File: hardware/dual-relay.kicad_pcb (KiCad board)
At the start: 2 copper layers, 45 x 45 mm, 38 parts, among them J101 AKL_5_2, J102 AKL_5_2, J103 AKL_5_2, P101 CON-SENSOR2, P102 BOOT, Q101 2N7002P, Q102 2N7002P, U101 XMC1XXX24, U102 DRILL, U103 DRILL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

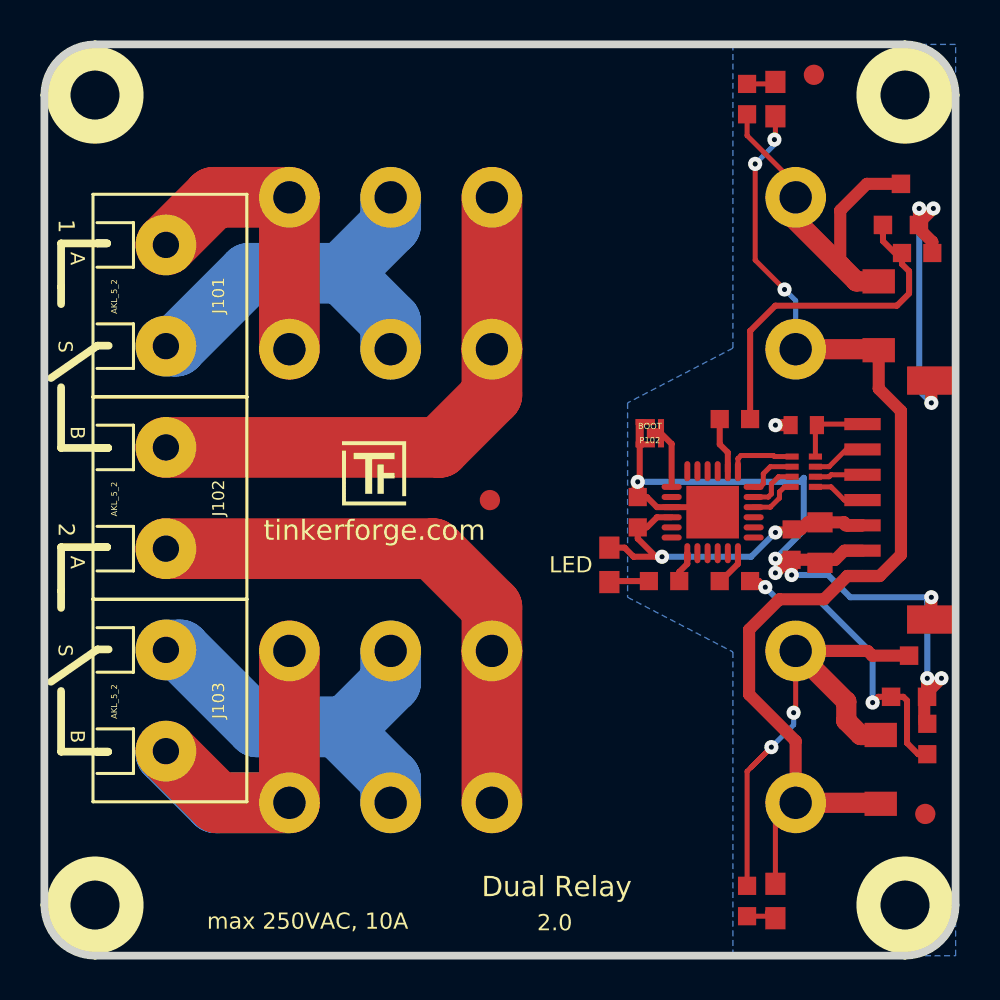
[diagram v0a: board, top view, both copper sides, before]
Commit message: industrial dual relay bricklet prototype finished
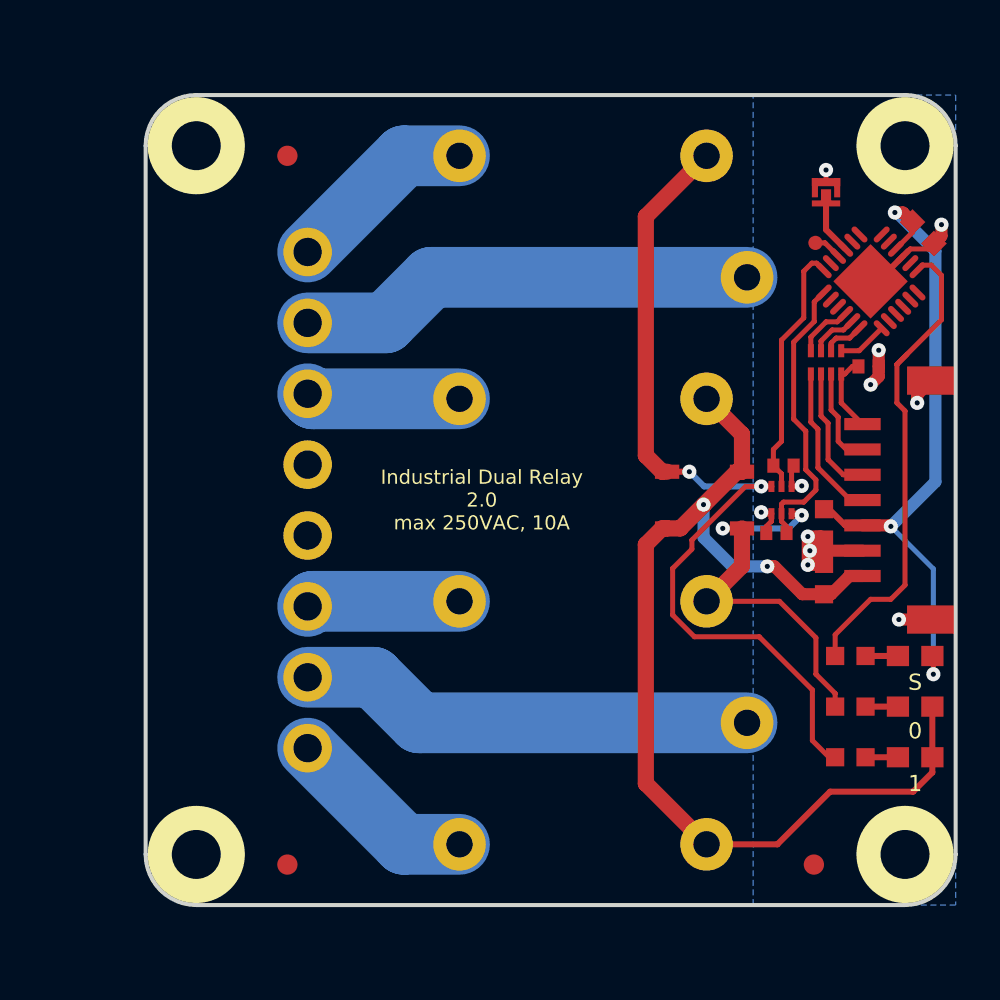
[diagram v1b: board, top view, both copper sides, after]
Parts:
- removed C101: 1uF, C0603F
- removed C102: 1uF, C0402E
- removed C103: 10uF, C0805
- removed C104: 100nF, C0603F
- removed D101, D104, D105: blue, D0603E
- removed D102, D103: LL4148, MiniMelf
- removed the Fiducial_Mark at (170.6, 119.7)
- removed the Fiducial_Mark at (165.1, 83.2)
- removed the Fiducial_Mark at (149.1, 104.2)
- removed the G*** at (160.6, 104.2)
- removed J101, J102, J103: AKL_5_2, AKL_5_2
- removed P101: CON-SENSOR2, kicad-libraries:CON-SENSOR2
- removed P102: BOOT, kicad-libraries:SolderJumper
- removed Q101, Q102: 2N7002P, SOT23GDS
- removed R101, R106, R107: 1k, R0603F
- removed R102, R103: 10, R0603F
- removed R104, R105: 10k, R0603F
- removed REL101, REL102: RELAY_29_127, RELAY_29_127
- removed RP101: TBD, kicad-libraries:4X0402
- removed U101: XMC1XXX24, kicad-libraries:QFN24-4x4mm-0.5mm
- removed U102, U103, U104, U105: DRILL, DRILL_NP
- added C1: 1uF, C0603F, F.Cu at (165.6, 108.1)
- added C2: 1uF, C0402F, F.Cu at (167.8, 97.6)
- added C3: 1uF, C0603F, F.Cu at (165.6, 105.4)
- added C4: 100nF, C0603F, F.Cu at (170.5, 91.0)
- added D1: blue, D0603E, F.Cu at (170.1, 111.9)
- added D2: blue, D0603E, F.Cu at (170.1, 116.9)
- added D3: blue, D0603E, F.Cu at (170.1, 114.4)
- added D4: LL4148, SOD-123, F.Cu at (159.7, 102.8)
- added D5: LL4148, SOD-123, F.Cu at (159.7, 105.6)
- added Fiducial_Mark: VAL**, kicad-libraries:Fiducial_Mark, F.Cu at (139.1, 87.2)
- added Fiducial_Mark: VAL**, kicad-libraries:Fiducial_Mark, F.Cu at (165.1, 122.2)
- added Fiducial_Mark: VAL**, kicad-libraries:Fiducial_Mark, F.Cu at (139.1, 122.2)
- added P1: CON-SENSOR2, CON-SENSOR2, F.Cu at (172.1, 104.2)
- added P2: BOOT, kicad-libraries:SolderJumper, F.Cu at (165.7, 89.0)
- added P3: CONN_8, kicad-libraries:OQ_8P, F.Cu at (140.1, 104.2)
- added P4: Debug, kicad-libraries:DEBUG_PAD, F.Cu at (165.2, 91.5)
- added Q1: SSM6N7002KFU, kicad-libraries:SOT563, F.Cu at (163.5, 104.2)
- added R1: 1k, R0603F, F.Cu at (166.9, 111.9)
- added R2: 1k, R0603F, F.Cu at (166.9, 116.9)
- added R3: 1k, R0603F, F.Cu at (166.9, 114.4)
- added R4: 10k, kicad-libraries:R0402F, F.Cu at (163.2, 105.8)
- added R5: 10k, kicad-libraries:R0402F, F.Cu at (163.6, 102.5)
- added RP1: TBD, kicad-libraries:4X0402, F.Cu at (165.7, 97.4)
- added U1: XMC1XXX24, kicad-libraries:QFN24-4x4mm-0.5mm, F.Cu at (167.9, 93.4)
- added U2: G5LE-1-36, G5LE-1, F.Cu at (153.1, 93.2)
- added U3: G5LE-1-36, G5LE-1, F.Cu at (153.1, 115.2)
- added U4: DRILL, DRILL_NP, F.Cu at (169.6, 121.7)
- added U5: DRILL, DRILL_NP, F.Cu at (134.6, 121.7)
- added U6: DRILL, DRILL_NP, F.Cu at (134.6, 86.7)
- added U7: DRILL, DRILL_NP, F.Cu at (169.6, 86.7)
- added VAL: WEEE_7mm, kicad-libraries:WEEE_7mm, B.Cu at (152.1, 108.2)
- G***: moved to B.Cu
- moved G*** 17.7 mm to (153.7, 114.4), turned to 180 degrees
- moved G*** 13.0 mm to (152.1, 91.2)
- moved VAL 10.3 mm to (152.1, 100.2)
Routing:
- net Net-(D4-Pad1): track 0.00 -> 44.5 mm, vias 0 -> 2
- net GND: track 61.8 -> 28.2 mm
- net Net-(J102-Pad1): track 27.0 -> 0.00 mm
- net Net-(J102-Pad2): track 26.9 -> 0.00 mm
- net Net-(D103-Pad1): track 26.2 -> 0.00 mm, vias 2 -> 0
- net Net-(R1-Pad1): track 0.00 -> 24.1 mm
- net Net-(P3-Pad7): track 0.00 -> 22.6 mm
- net Net-(P3-Pad2): track 0.00 -> 22.6 mm
- net Net-(J103-Pad1): track 21.9 -> 0.00 mm
- net Net-(D5-Pad1): track 0.00 -> 20.8 mm, vias 0 -> 2
- net Net-(J103-Pad2): track 20.0 -> 0.00 mm
- net Net-(J101-Pad1): track 19.7 -> 0.00 mm
- net Net-(D102-Pad1): track 18.0 -> 0.00 mm
- net Net-(Q101-PadG): track 17.2 -> 0.00 mm
- net Net-(Q102-PadG): track 15.4 -> 0.00 mm, vias 2 -> 0
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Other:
- board size 45 x 45 mm -> 40 x 40 mm
- board text added: "0"
- board text added: "Industrial Dual Relay 2.0 max 250VAC, 10A"
- board text removed: "2"
- board text removed: "2.0"
- board text removed: "Dual Relay"
- board text removed: "LED"
- board text removed: "max 250VAC, 10A"

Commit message: fix description text
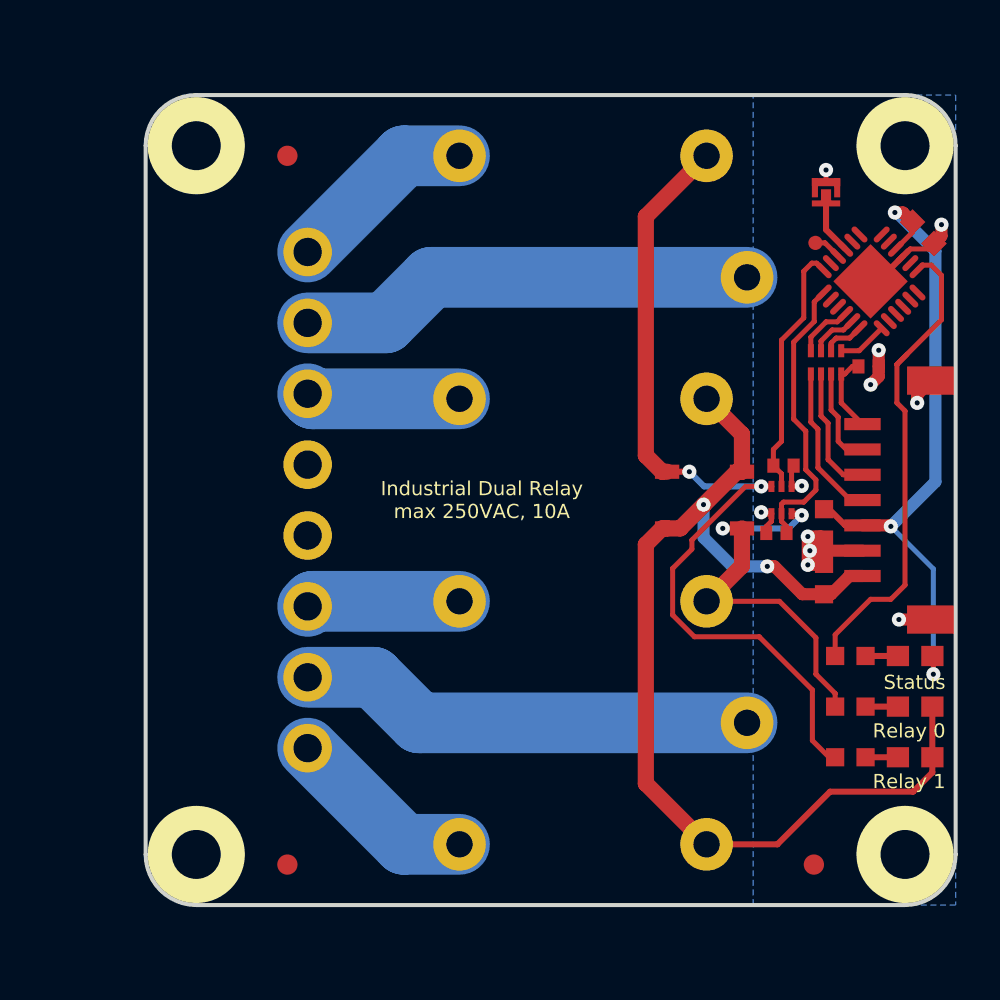
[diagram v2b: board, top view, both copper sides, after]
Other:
- board text added: "Industrial Dual Relay max 250VAC, 10A"
- board text added: "Relay 0"
- board text added: "Relay 1"
- board text added: "Status"
- board text removed: "Industrial Dual Relay 2.0 max 250VAC, 10A"
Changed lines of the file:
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@@
     (links 61)
     (no_connects 0)
-    (area 131.973659 84.071159 172.175001 124.275001)
+    (area 131.220139 83.320139 282.19527 165.489573)
     (thickness 1.6002)
     (drawings 34)
@@
   (layers
     (0 Vorderseite signal)
-    (31 Rückseite signal)
+    (31 Rückseite signal hide)
     (32 B.Adhes user)
     (33 F.Adhes user)
@@
   (gr_line (start 136.075 109.475) (end 133.675 109.475) (angle 90) (layer B.SilkS) (width 0.381))
   (gr_line (start 135.5 112.975) (end 134.15 114.325) (angle 90) (layer B.SilkS) (width 0.381))
-  (gr_text S (at 170.075 113.175) (layer F.SilkS)
-    (effects (font (size 0.8001 0.8001) (thickness 0.14986)))
+  (gr_text Status (at 171.575 113.175) (layer F.SilkS)
+    (effects (font (size 0.7 0.7) (thickness 0.14986)) (justify right))
   )
-  (gr_text 1 (at 170.075 118.175) (layer F.SilkS)
-    (effects (font (size 0.8001 0.8001) (thickness 0.14986)))
+  (gr_text "Relay 1" (at 171.575 118.075) (layer F.SilkS)
+    (effects (font (size 0.7 0.7) (thickness 0.14986)) (justify right))
   )
   (gr_line (start 172.075 121.675) (end 172.075 86.675) (angle 90) (layer Edge.Cuts) (width 0.2))
@@
   (gr_line (start 132.075 86.675) (end 132.075 121.675) (angle 90) (layer Edge.Cuts) (width 0.2))
   (gr_line (start 169.575 84.175) (end 134.575 84.175) (angle 90) (layer Edge.Cuts) (width 0.2))
-  (gr_text 0 (at 170.075 115.575) (layer F.SilkS)
-    (effects (font (size 0.8001 0.8001) (thickness 0.14986)))
+  (gr_text "Relay 0" (at 171.575 115.575) (layer F.SilkS)
+    (effects (font (size 0.7 0.7) (thickness 0.14986)) (justify right))
   )
   (gr_text A (at 134.475 110.175 270) (layer B.SilkS)
@@
   (gr_arc (start 169.57294 121.67298) (end 172.0723 121.67298) (angle 90) (layer Edge.Cuts) (width 0.2))
   (gr_arc (start 169.57294 86.67306) (end 169.57294 84.17116) (angle 90) (layer Edge.Cuts) (width 0.2))
-  (gr_text "Industrial Dual Relay\n2.0\nmax 250VAC, 10A" (at 148.675 104.175) (layer F.SilkS)
+  (gr_text "Industrial Dual Relay\nmax 250VAC, 10A" (at 148.675 104.175) (layer F.SilkS)
     (effects (font (size 0.7 0.7) (thickness 0.15)))
   )

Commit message: specify values
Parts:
- C2: value 1uF -> 220pF
- RP1: value TBD -> 82
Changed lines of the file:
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@@
     (links 61)
     (no_connects 0)
-    (area 131.220139 83.320139 282.19527 165.489573)
+    (area 131.973659 84.071159 172.175001 124.275001)
     (thickness 1.6002)
     (drawings 34)
@@
       (effects (font (size 0.2 0.2) (thickness 0.05)))
     )
-    (fp_text value TBD (at -0.025 -0.45) (layer F.Fab)
+    (fp_text value 82 (at -0.025 -0.45) (layer F.Fab)
       (effects (font (size 0.2 0.2) (thickness 0.05)))
     )
@@
       (effects (font (size 0.2 0.2) (thickness 0.05)))
     )
-    (fp_text value 1uF (at 0 -0.15 180) (layer F.Fab)
-      (effects (font (size 0.2 0.2) (thickness 0.05)))
-    )
+    (fp_text value 220pF (at 0 -0.15 180) (layer F.Fab)
+      (effects (font (size 0.2 0.2) (thickness 0.05)))
+    )

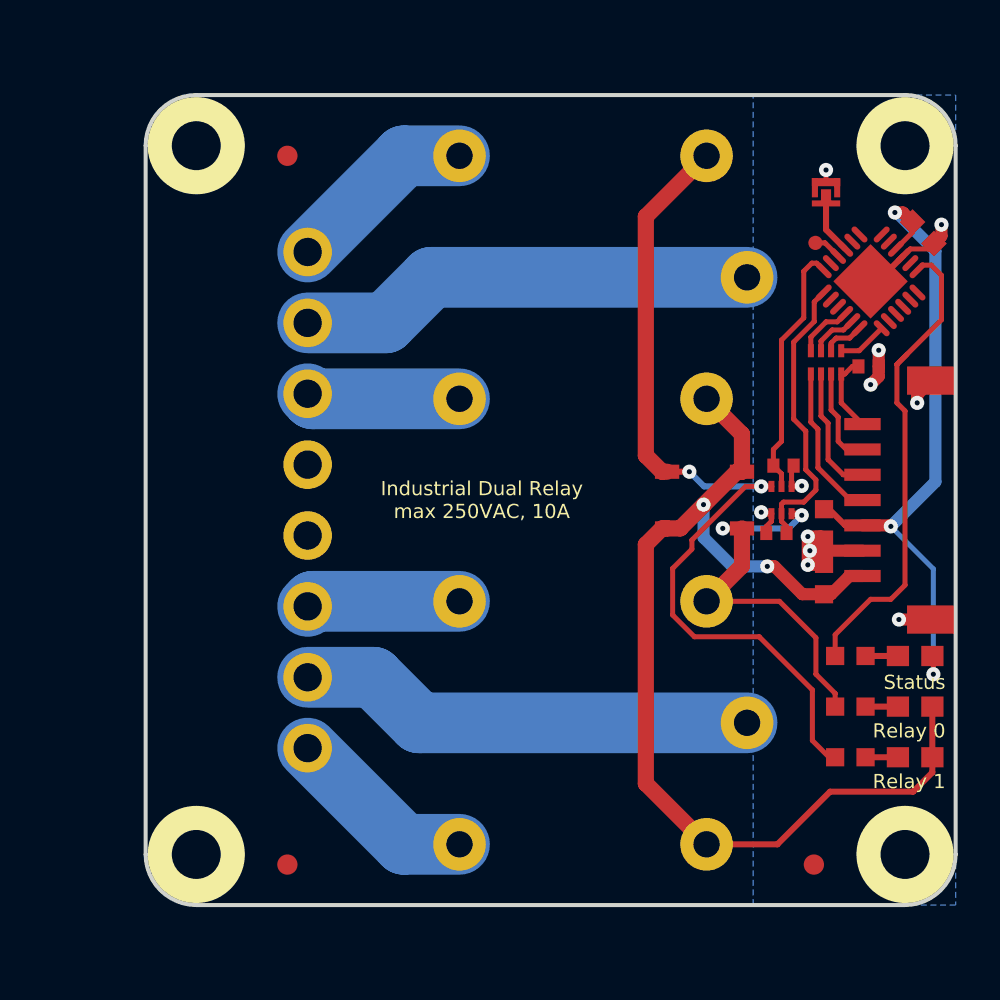
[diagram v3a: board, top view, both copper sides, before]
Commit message: fix mosfet footprint
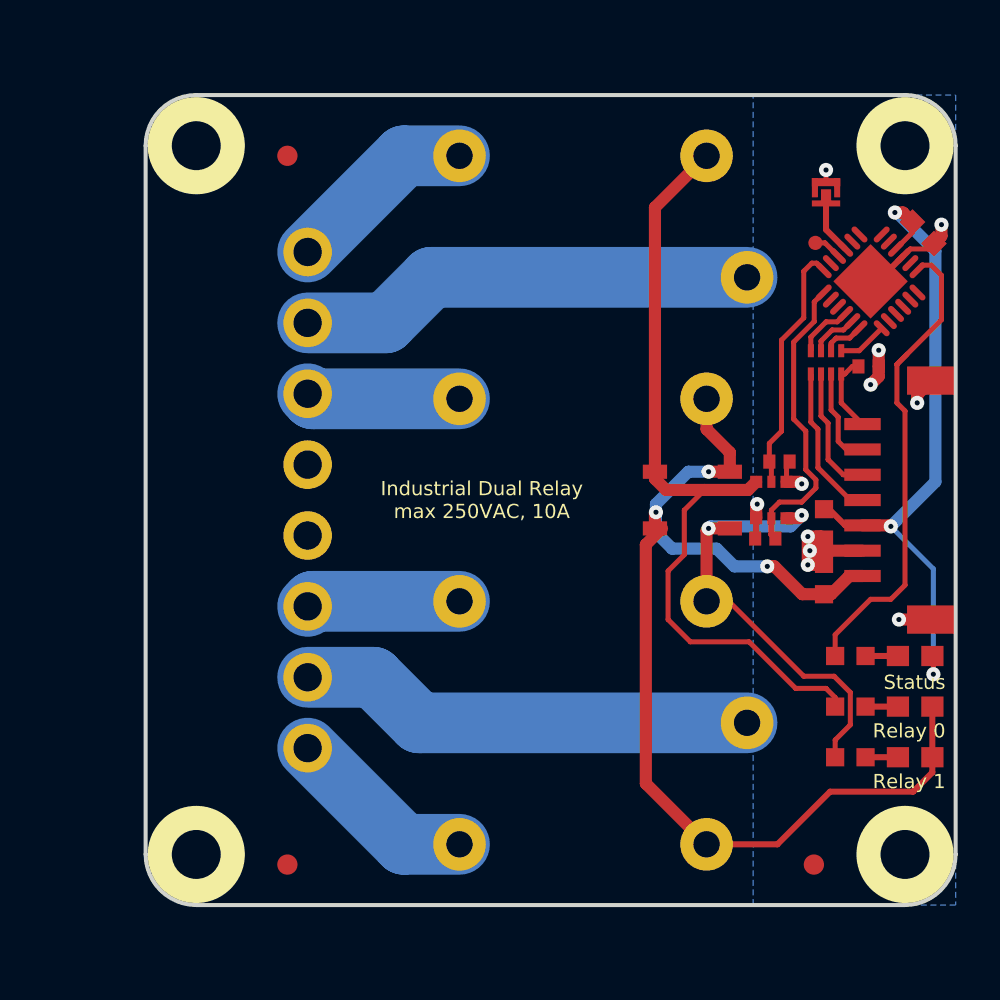
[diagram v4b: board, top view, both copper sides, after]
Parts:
- Q1: footprint kicad-libraries:SOT563 -> kicad-libraries:SOT363
- R4, R5: footprint kicad-libraries:R0402F -> R0402F
- moved D2 2.50 mm to (170.1, 114.4)
- moved D3 2.50 mm to (170.1, 116.9)
- moved R2 2.50 mm to (166.9, 114.4)
- moved R3 2.50 mm to (166.9, 116.9)
- moved R4 0.61 mm to (162.7, 106.1)
- moved D4 0.60 mm to (159.1, 102.8)
- moved D5 0.60 mm to (159.1, 105.6)
- moved Q1 0.50 mm to (163.0, 104.2), turned to 90 degrees
- moved R5 0.28 mm to (163.4, 102.3)
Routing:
- net Net-(D5-Pad1): track 20.8 -> 25.9 mm
- net Net-(D4-Pad1): track 44.5 -> 39.8 mm, vias 2 -> 0
- net +5V: track 53.5 -> 55.5 mm, vias 2 -> 3
- net RELAY1: track 14.3 -> 14.9 mm

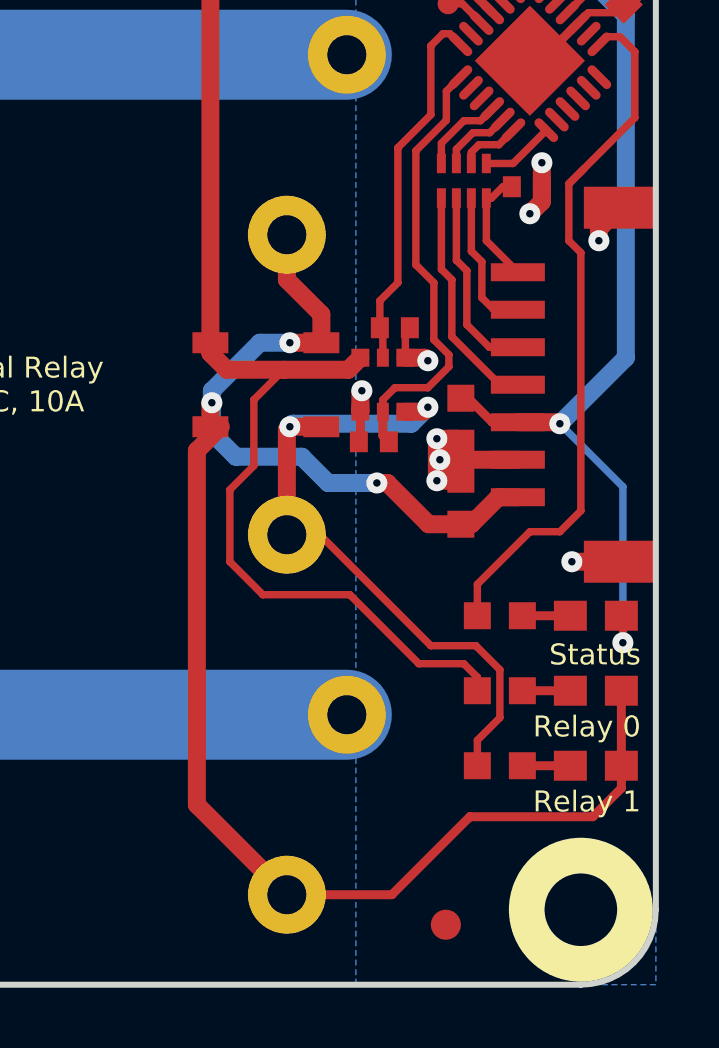
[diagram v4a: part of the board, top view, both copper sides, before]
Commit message: fix logo positions
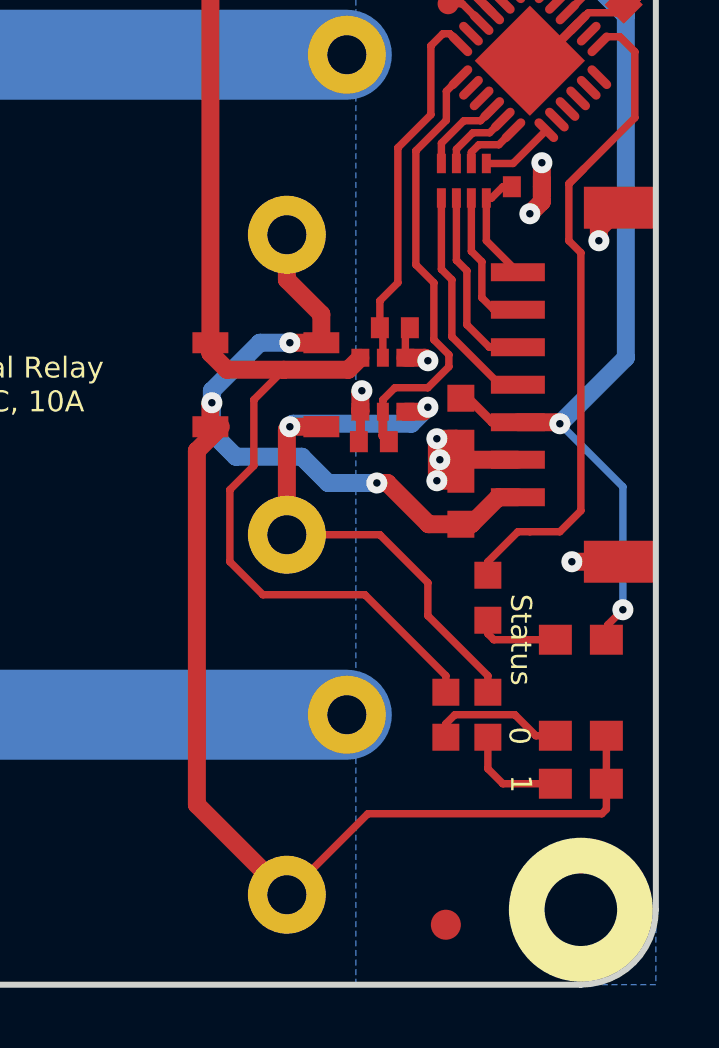
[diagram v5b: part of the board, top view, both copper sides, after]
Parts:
- moved G*** 23.0 mm to (152.1, 114.2), turned to 90 degrees
- moved G*** 18.8 mm to (170.4, 105.8), turned to 90 degrees
- moved VAL 6.00 mm to (152.1, 94.2), turned to 90 degrees
- moved VAL 4.00 mm to (152.1, 104.2), turned to 90 degrees
- moved R2 1.97 mm to (165.1, 115.2), turned to 270 degrees
- moved R3 1.75 mm to (166.5, 115.2), turned to 270 degrees
- moved D2 1.58 mm to (169.6, 115.9)
- moved D1 0.94 mm to (169.6, 112.7)
- moved D3 0.78 mm to (169.6, 117.5)
- moved R1 0.72 mm to (166.5, 111.3), turned to 270 degrees
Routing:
- net Net-(D2-Pad2): track 1.60 -> 4.51 mm
- net Net-(D3-Pad2): track 1.60 -> 3.51 mm
- net +5V: track 55.5 -> 53.9 mm
- net Net-(D5-Pad1): track 25.9 -> 24.4 mm
- net Net-(R1-Pad1): track 24.1 -> 22.8 mm
- net Net-(D1-Pad2): track 1.60 -> 2.78 mm
- net Net-(D4-Pad1): track 39.8 -> 38.9 mm
- net VCC: track 32.9 -> 32.1 mm
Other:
- board text removed: "Relay 0"
- board text removed: "Relay 1"
